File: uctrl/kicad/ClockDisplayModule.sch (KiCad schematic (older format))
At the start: 10 parts, among them IC1 ATMEGA88PA-A, P101 CONN_02X03, P102 CONN_01X06, SW101 TL3315NF160Q

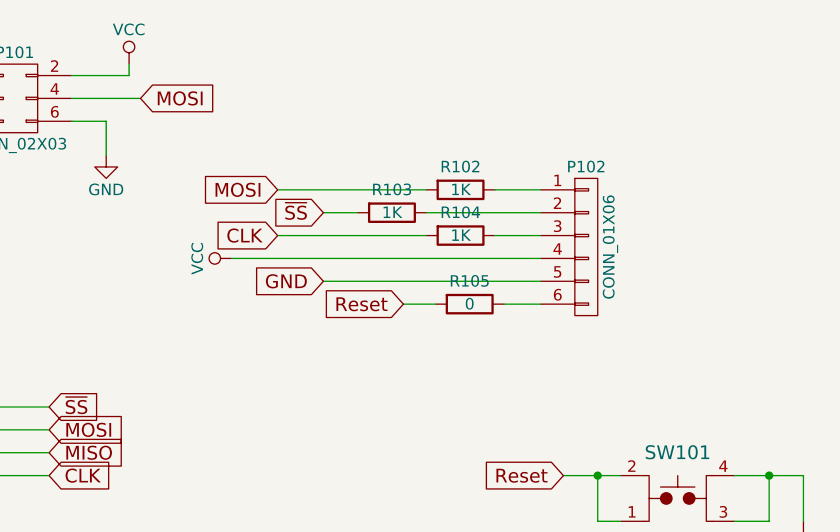
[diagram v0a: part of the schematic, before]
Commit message: Altered the pin header to include MISO and to simplify connection to to the main board.
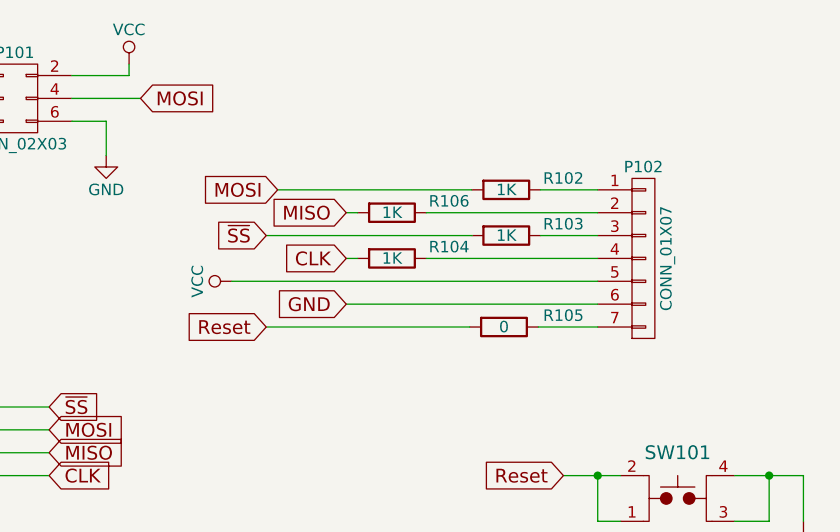
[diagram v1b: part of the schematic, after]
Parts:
- removed P102: CONN_01X06, Pin_Headers:Pin_Header_Straight_1x06, symbol CONN_01X06
- added P102: CONN_01X07, Pin_Headers:Pin_Header_Straight_1x07, symbol CONN_01X07
- added R106: 1K, Resistors_SMD:R_0805, symbol R
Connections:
- net GND: now also P102.6 (P6)
- net MISO: now also R106.2
- net VCC: now also P102.5 (P5)
- net at R102.1: now also P102.1 (P1)
- net at R103.1: now also P102.3 (P3)
- net at R104.1: now also P102.4 (P4)
- net at R105.1: now also P102.7 (P7)
- new net: P102.2 (P2), R106.1
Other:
- moved on the sheet: R102, R103, R104, R105
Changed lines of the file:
@@
 Text GLabel 6000 1450 0    60   Input ~ 0
 MOSI
-Text GLabel 6200 1550 0    60   Input ~ 0
+Text GLabel 5950 1650 0    60   Input ~ 0
 ~SS
-Text GLabel 6000 1650 0    60   Input ~ 0
+Text GLabel 6300 1750 0    60   Input ~ 0
 CLK
-Text GLabel 6200 1850 0    60   Input ~ 0
+Text GLabel 6300 1950 0    60   Input ~ 0
 GND
 $Comp
@@
 L VCC #PWR03
 U 1 1 5586896F
-P 5800 1750
-F 0 "#PWR03" H 5800 1600 50  0001 C CNN
-F 1 "VCC" H 5800 1900 50  0000 C CNN
-F 2 "" H 5800 1750 60  0000 C CNN
-F 3 "" H 5800 1750 60  0000 C CNN
-	1    5800 1750
+P 5800 1850
+F 0 "#PWR03" H 5800 1700 50  0001 C CNN
+F 1 "VCC" H 5800 2000 50  0000 C CNN
+F 2 "" H 5800 1850 60  0000 C CNN
+F 3 "" H 5800 1850 60  0000 C CNN
+	1    5800 1850
 	0    -1   -1   0
 $EndComp
@@
 L R R102
 U 1 1 5660E284
-P 6800 1450
-F 0 "R102" V 6700 1450 50  0000 C CNN
-F 1 "1K" V 6800 1450 50  0000 C CNN
-F 2 "Resistors_SMD:R_0805" V 6730 1450 30  0001 C CNN
-F 3 "" H 6800 1450 30  0000 C CNN
-	1    6800 1450
+P 7000 1450
+F 0 "R102" V 6950 1700 50  0000 C CNN
+F 1 "1K" V 7000 1450 50  0000 C CNN
+F 2 "Resistors_SMD:R_0805" V 6930 1450 30  0001 C CNN
+F 3 "" H 7000 1450 30  0000 C CNN
+	1    7000 1450
 	0    1    1    0
 $EndComp
@@
 L R R103
 U 1 1 5660E384
-P 6500 1550
-F 0 "R103" V 6400 1550 50  0000 C CNN
-F 1 "1K" V 6500 1550 50  0000 C CNN
-F 2 "Resistors_SMD:R_0805" V 6430 1550 30  0001 C CNN
-F 3 "" H 6500 1550 30  0000 C CNN
-	1    6500 1550
+P 7000 1650
+F 0 "R103" V 6950 1900 50  0000 C CNN
+F 1 "1K" V 7000 1650 50  0000 C CNN
+F 2 "Resistors_SMD:R_0805" V 6930 1650 30  0001 C CNN
+F 3 "" H 7000 1650 30  0000 C CNN
+	1    7000 1650
 	0    1    1    0
 $EndComp
@@
 L R R104
 U 1 1 5660E3C8
-P 6800 1650
-F 0 "R104" V 6700 1650 50  0000 C CNN
-F 1 "1K" V 6800 1650 50  0000 C CNN
-F 2 "Resistors_SMD:R_0805" V 6730 1650 30  0001 C CNN
-F 3 "" H 6800 1650 30  0000 C CNN
-	1    6800 1650
-	0    1    1    0
-$EndComp
-$Comp
-L CONN_01X06 P102
-U 1 1 5660E685
-P 7350 1700
-F 0 "P102" H 7350 2050 50  0000 C CNN
-F 1 "CONN_01X06" V 7450 1700 50  0000 C CNN
-F 2 "Pin_Headers:Pin_Header_Straight_1x06" H 7350 1700 60  0001 C CNN
-F 3 "" H 7350 1700 60  0000 C CNN
-	1    7350 1700
-	1    0    0    -1
-$EndComp
-Text GLabel 6550 1950 0    60   Input ~ 0
+P 6500 1750
+F 0 "R104" V 6450 2000 50  0000 C CNN
+F 1 "1K" V 6500 1750 50  0000 C CNN
+F 2 "Resistors_SMD:R_0805" V 6430 1750 30  0001 C CNN
+F 3 "" H 6500 1750 30  0000 C CNN
+	1    6500 1750
+	0    1    1    0
+$EndComp
+Text GLabel 5950 2050 0    60   Input ~ 0
 Reset
 Text GLabel 7250 2700 0    60   Input ~ 0
@@
 L R R105
 U 1 1 56DAA348
-P 6840 1950
-F 0 "R105" V 6740 1950 50  0000 C CNN
-F 1 "0" V 6840 1950 50  0000 C CNN
-F 2 "Resistors_SMD:R_0805" V 6770 1950 30  0001 C CNN
-F 3 "" H 6840 1950 30  0000 C CNN
-	1    6840 1950
+P 6990 2050
+F 0 "R105" V 6940 2310 50  0000 C CNN
+F 1 "0" V 6990 2050 50  0000 C CNN
+F 2 "Resistors_SMD:R_0805" V 6920 2050 30  0001 C CNN
+F 3 "" H 6990 2050 30  0000 C CNN
+	1    6990 2050
 	0    1    1    0
 $EndComp
@@
 	4750 4100 5100 4100
 Wire Wire Line
-	5800 1750 7150 1750
-Wire Wire Line
-	6200 1850 7150 1850
+	5800 1850 7400 1850
+Wire Wire Line
+	6300 1950 7400 1950
 Wire Wire Line
 	5000 3050 4750 3050
@@
 	6450 3650 6150 3650
 Wire Wire Line
-	6000 1450 6650 1450
-Wire Wire Line
-	6950 1450 7150 1450
-Wire Wire Line
-	7150 1550 6650 1550
-Wire Wire Line
-	6350 1550 6200 1550
-Wire Wire Line
-	6000 1650 6650 1650
-Wire Wire Line
-	6950 1650 7150 1650
+	6000 1450 6850 1450
+Wire Wire Line
+	7150 1450 7400 1450
+Wire Wire Line
+	7400 1650 7150 1650
+Wire Wire Line
+	6850 1650 5950 1650
+Wire Wire Line
+	6300 1750 6350 1750
+Wire Wire Line
+	6650 1750 7400 1750
 Wire Wire Line
 	2250 1750 2250 2200
@@
 Connection ~ 7400 2700
 Wire Wire Line
-	6550 1950 6690 1950
-Wire Wire Line
-	6990 1950 7150 1950
+	5950 2050 6840 2050
+Wire Wire Line
+	7140 2050 7400 2050
+$Comp
+L CONN_01X07 P102
+U 1 1 579A8A73
+P 7600 1750
+F 0 "P102" H 7600 2150 50  0000 C CNN
+F 1 "CONN_01X07" V 7700 1750 50  0000 C CNN
+F 2 "Pin_Headers:Pin_Header_Straight_1x07" H 7600 1750 50  0001 C CNN
+F 3 "" H 7600 1750 50  0000 C CNN
+F 4 "Value" H 7600 1750 60  0001 C CNN "DigiKeyPN"
+F 5 "Value" H 7600 1750 60  0001 C CNN "Voltage"
+F 6 "Value" H 7600 1750 60  0001 C CNN "ConradPN"
+F 7 "Value" H 7600 1750 60  0001 C CNN "Link"
+F 8 "No" H 7600 1750 60  0001 C CNN "On-Hand"
+	1    7600 1750
+	1    0    0    -1
+$EndComp
+Text GLabel 6300 1550 0    60   Input ~ 0
+MISO
+$Comp
+L R R106
+U 1 1 579A8CCF
+P 6500 1550
+F 0 "R106" V 6450 1800 50  0000 C CNN
+F 1 "1K" V 6500 1550 50  0000 C CNN
+F 2 "Resistors_SMD:R_0805" V 6430 1550 30  0001 C CNN
+F 3 "" H 6500 1550 30  0000 C CNN
+	1    6500 1550
+	0    1    1    0
+$EndComp
+Wire Wire Line
+	6300 1550 6350 1550
+Wire Wire Line
+	6650 1550 7400 1550
 $EndSCHEMATC
